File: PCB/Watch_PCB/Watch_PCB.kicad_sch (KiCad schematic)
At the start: 54 parts, among them IC1 PCF2003DUS, IC2 BMM350, IC3 STM32L011E4Y6TR, IC4 TPS22919DCKR, Q11 2N7002KQBZ, Q12 2N7002KQBZ, Q3 2N7002KQBZ, Q4 2N7002KQBZ, Q5 2N7002KQBZ, Q6 2N7002KQBZ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

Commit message: added debounce on switch
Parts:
- added C12: 220n, Capacitor_SMD:C_0201_0603Metric, symbol Device:C
- added R18: 47k, Resistor_SMD:R_0201_0603Metric, symbol Device:R
- R17: value 10k -> 1k
- renumbered CLPT to CLPT1, CSPT to CSPT1
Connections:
- net GND: now also C12.1
- net GPIO_EXTI9: now also R18.2; no longer R17.2, SW5.3 (K), SW5.4 (A)
- new net: C12.2, R17.2, R18.1, SW5.3 (K), SW5.4 (A)
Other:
- moved on the sheet: R17, SW5

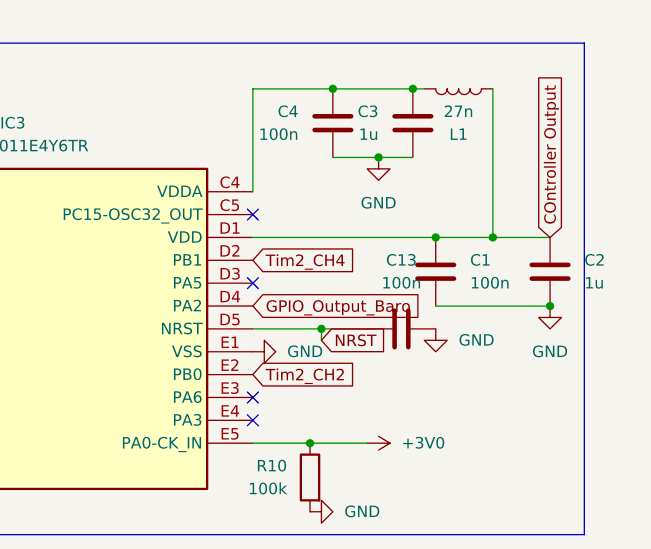
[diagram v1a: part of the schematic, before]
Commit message: pcb outline
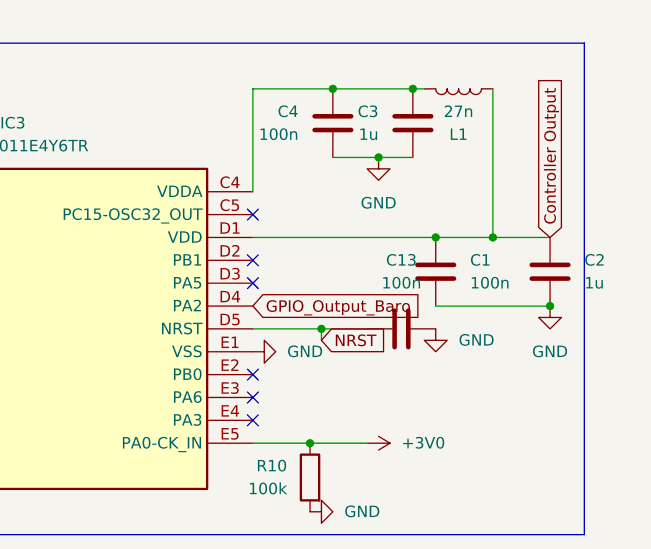
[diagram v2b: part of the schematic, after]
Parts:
- IC4: footprint SOT65P210X110-6N -> SamacSys_Parts:SOT65P210X110-6N
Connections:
- net COntroller Output is gone; now on net Controller Output: C1.2, C2.2, IC3.D1 (VDD), L1.1
- net Tim2_CH2: no longer names the net of IC3.E2 (PB0)
- net Tim2_CH4: no longer names the net of IC3.D2 (PB1)
- no-connect marks 10 -> 12
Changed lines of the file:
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@@
+	)
+	(no_connect
+		(at 241.3 39.37)
 	)
 	(no_connect
@@
 	)
 	(no_connect
+		(at 241.3 52.07)
+	)
+	(no_connect
 		(at 121.92 182.88)
 	)
@@
 		)
 	)
+	(global_label "Controller Output"
+		(shape input)
+		(at 274.32 36.83 90)
+		(fields_autoplaced yes)
+		(effects
+			(font
+				(size 1.27 1.27)
+			)
+			(justify left)
+		)
+		(property "Intersheetrefs" "${INTERSHEET_REFS}"
+			(at 274.32 17.2142 90)
+			(effects
+				(font
+					(size 1.27 1.27)
+				)
+				(justify left)
+				(hide yes)
+			)
+		)
+	)
 	(global_label "SYS_SWCLK"
 		(shape input)
@@
 		)
 	)
-	(global_label "COntroller Output"
-		(shape input)
-		(at 274.32 36.83 90)
+	(global_label "BaroVCC"
+		(shape input)
+		(at 240.03 77.47 0)
 		(fields_autoplaced yes)
 		(effects
@@
 		)
 		(property "Intersheetrefs" "${INTERSHEET_REFS}"
-			(at 274.32 17.0327 90)
+			(at 250.998 77.47 0)
 			(effects
 				(font
@@
 		)
 	)
-	(global_label "BaroVCC"
-		(shape input)
-		(at 240.03 77.47 0)
+	(global_label "OSCIN"
+		(shape input)
+		(at 121.92 187.96 180)
+		(fields_autoplaced yes)
+		(effects
+			(font
+				(size 1.27 1.27)
+			)
+			(justify right)
+		)
+		(property "Intersheetrefs" "${INTERSHEET_REFS}"
+			(at 113.1895 187.96 0)
+			(effects
+				(font
+					(size 1.27 1.27)
+				)
+				(justify right)
+				(hide yes)
+			)
+		)
+	)
+	(global_label "GPIO_EXTI1"
+		(shape input)
+		(at 237.49 137.16 0)
 		(fields_autoplaced yes)
 		(effects
@@
 		)
 		(property "Intersheetrefs" "${INTERSHEET_REFS}"
-			(at 250.998 77.47 0)
+			(at 251.0585 137.16 0)
 			(effects
 				(font
@@
 		)
 	)
+	(global_label "GPIO_EXTI9"
+		(shape input)
+		(at 187.96 41.91 180)
+		(fields_autoplaced yes)
+		(effects
+			(font
+				(size 1.27 1.27)
+			)
+			(justify right)
+		)
+		(property "Intersheetrefs" "${INTERSHEET_REFS}"
+			(at 174.3915 41.91 0)
+			(effects
+				(font
+					(size 1.27 1.27)
+				)
+				(justify right)
+				(hide yes)
+			)
+		)
+	)
+	(global_label "SYS_SWCLK"
+		(shape input)
+		(at 187.96 34.29 180)
+		(fields_autoplaced yes)
+		(effects
+			(font
+				(size 1.27 1.27)
+			)
+			(justify right)
+		)
+		(property "Intersheetrefs" "${INTERSHEET_REFS}"
+			(at 174.2706 34.29 0)
+			(effects
+				(font
+					(size 1.27 1.27)
+				)
+				(justify right)
+				(hide yes)
+			)
+		)
+	)
+	(global_label "GPIO_EXTI9"
+		(shape input)
+		(at 204.47 138.43 0)
+		(fields_autoplaced yes)
+		(effects
+			(font
+				(size 1.27 1.27)
+			)
+			(justify left)
+		)
+		(property "Intersheetrefs" "${INTERSHEET_REFS}"
+			(at 218.0385 138.43 0)
+			(effects
+				(font
+					(size 1.27 1.27)
+				)
+				(justify left)
+				(hide yes)
+			)
+		)
+	)
+	(global_label "Controller Output"
+		(shape input)
+		(at 279.4 130.81 180)
+		(fields_autoplaced yes)
+		(effects
+			(font
+				(size 1.27 1.27)
+			)
+			(justify right)
+		)
+		(property "Intersheetrefs" "${INTERSHEET_REFS}"
+			(at 259.7842 130.81 0)
+			(effects
+				(font
+					(size 1.27 1.27)
+				)
+				(justify right)
+				(hide yes)
+			)
+		)
+	)
+	(global_label "Tim2_CH1"
+		(shape input)
+		(at 158.75 49.53 180)
+		(fields_autoplaced yes)
+		(effects
+			(font
+				(size 1.27 1.27)
+			)
+			(justify right)
+		)
+		(property "Intersheetrefs" "${INTERSHEET_REFS}"
+			(at 146.512 49.53 0)
+			(effects
+				(font
+					(size 1.27 1.27)
+				)
+				(justify right)
+				(hide yes)
+			)
+		)
+	)
 	(global_label "OSCIN"
 		(shape input)
-		(at 121.92 187.96 180)
+		(at 121.92 161.29 180)
 		(fields_autoplaced yes)
 		(effects
@@
 		)
 		(property "Intersheetrefs" "${INTERSHEET_REFS}"
-			(at 113.1895 187.96 0)
+			(at 113.1895 161.29 0)
 			(effects
 				(font
@@
 		)
 	)
-	(global_label "GPIO_EXTI1"
-		(shape input)
-		(at 237.49 137.16 0)
+	(global_label "SYS_SWDIO"
+		(shape input)
+		(at 152.4 21.59 180)
+		(fields_autoplaced yes)
+		(effects
+			(font
+				(size 1.27 1.27)
+			)
+			(justify right)
+		)
+		(property "Intersheetrefs" "${INTERSHEET_REFS}"
+			(at 139.0734 21.59 0)
+			(effects
+				(font
+					(size 1.27 1.27)
+				)
+				(justify right)
+				(hide yes)
+			)
+		)
+	)
+	(global_label "GPIO_Output_Comp"
+		(shape input)
+		(at 135.89 93.98 0)
 		(fields_autoplaced yes)
 		(effects
@@
 		)
 		(property "Intersheetrefs" "${INTERSHEET_REFS}"
-			(at 251.0585 137.16 0)
-			(effects
-				(font
-					(size 1.27 1.27)
-				)
-				(justify left)
-				(hide yes)
-			)
-		)
-	)
-	(global_label "GPIO_EXTI9"
-		(shape input)
-		(at 187.96 41.91 180)
-		(fields_autoplaced yes)
-		(effects
-			(font
-				(size 1.27 1.27)
-			)
-			(justify right)
-		)
-		(property "Intersheetrefs" "${INTERSHEET_REFS}"
-			(at 174.3915 41.91 0)
-			(effects
-				(font
-					(size 1.27 1.27)
-				)
-				(justify right)
-				(hide yes)
-			)
-		)
-	)
-	(global_label "SYS_SWCLK"
-		(shape input)
-		(at 187.96 34.29 180)
-		(fields_autoplaced yes)
-		(effects
-			(font
-				(size 1.27 1.27)
-			)
-			(justify right)
-		)
-		(property "Intersheetrefs" "${INTERSHEET_REFS}"
-			(at 174.2706 34.29 0)
-			(effects
-				(font
-					(size 1.27 1.27)
-				)
-				(justify right)
-				(hide yes)
-			)
-		)
-	)
-	(global_label "GPIO_EXTI9"
-		(shape input)
-		(at 204.47 138.43 0)
-		(fields_autoplaced yes)
-		(effects
-			(font
-				(size 1.27 1.27)
-			)
-			(justify left)
-		)
-		(property "Intersheetrefs" "${INTERSHEET_REFS}"
-			(at 218.0385 138.43 0)
-			(effects
-				(font
-					(size 1.27 1.27)
-				)
-				(justify left)
-				(hide yes)
-			)
-		)
-	)
-	(global_label "Controller Output"
-		(shape input)
-		(at 279.4 130.81 180)
-		(fields_autoplaced yes)
-		(effects
-			(font
-				(size 1.27 1.27)
-			)
-			(justify right)
-		)
-		(property "Intersheetrefs" "${INTERSHEET_REFS}"
-			(at 259.7842 130.81 0)
-			(effects
-				(font
-					(size 1.27 1.27)
-				)
-				(justify right)
-				(hide yes)
-			)
-		)
-	)
-	(global_label "Tim2_CH1"
-		(shape input)
-		(at 158.75 49.53 180)
-		(fields_autoplaced yes)
-		(effects
-			(font
-				(size 1.27 1.27)
-			)
-			(justify right)
-		)
-		(property "Intersheetrefs" "${INTERSHEET_REFS}"
-			(at 146.512 49.53 0)
-			(effects
-				(font
-					(size 1.27 1.27)
-				)
-				(justify right)
-				(hide yes)
-			)
-		)
-	)
-	(global_label "OSCIN"
-		(shape input)
-		(at 121.92 161.29 180)
-		(fields_autoplaced yes)
-		(effects
-			(font
-				(size 1.27 1.27)
-			)
-			(justify right)
-		)
-		(property "Intersheetrefs" "${INTERSHEET_REFS}"
-			(at 113.1895 161.29 0)
-			(effects
-				(font
-					(size 1.27 1.27)
-				)
-				(justify right)
-				(hide yes)
-			)
-		)
-	)
-	(global_label "SYS_SWDIO"
-		(shape input)
-		(at 152.4 21.59 180)
-		(fields_autoplaced yes)
-		(effects
-			(font
-				(size 1.27 1.27)
-			)
-			(justify right)
-		)
-		(property "Intersheetrefs" "${INTERSHEET_REFS}"
-			(at 139.0734 21.59 0)
-			(effects
-				(font
-					(size 1.27 1.27)
-				)
-				(justify right)
-				(hide yes)
-			)
-		)
-	)
-	(global_label "Tim2_CH2"
-		(shape input)
-		(at 241.3 52.07 0)
-		(fields_autoplaced yes)
-		(effects
-			(font
-				(size 1.27 1.27)
-			)
-			(justify left)
-		)
-		(property "Intersheetrefs" "${INTERSHEET_REFS}"
-			(at 253.538 52.07 0)
-			(effects
-				(font
-					(size 1.27 1.27)
-				)
-				(justify left)
-				(hide yes)
-			)
-		)
-	)
-	(global_label "GPIO_Output_Comp"
-		(shape input)
-		(at 135.89 93.98 0)
-		(fields_autoplaced yes)
-		(effects
-			(font
-				(size 1.27 1.27)
-			)
-			(justify left)
-		)
-		(property "Intersheetrefs" "${INTERSHEET_REFS}"
 			(at 156.7759 93.98 0)
-			(effects
-				(font
-					(size 1.27 1.27)
-				)
-				(justify left)
-				(hide yes)
-			)
-		)
-	)
-	(global_label "Tim2_CH4"
-		(shape input)
-		(at 241.3 39.37 0)
-		(fields_autoplaced yes)
-		(effects
-			(font
-				(size 1.27 1.27)
-			)
-			(justify left)
-		)
-		(property "Intersheetrefs" "${INTERSHEET_REFS}"
-			(at 253.538 39.37 0)
 			(effects
 				(font
@@
 			)
 		)
-		(property "Footprint" "SOT65P210X110-6N"
+		(property "Footprint" "SamacSys_Parts:SOT65P210X110-6N"
 			(at 267.97 237.16 0)
 			(effects

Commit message: pcb layout
pcb layout
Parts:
- removed IC4: TPS22919DCKR, SamacSys_Parts:SOT65P210X110-6N, symbol SamacSys_Parts:TPS22919DCKR
- removed Q11, Q12: 2N7002KQBZ, SamacSys_Parts:2N7002KQBZ, symbol SamacSys_Parts:2N7002KQBZ
- removed R6, R7: 2k, Resistor_SMD:R_0201_0603Metric, symbol Device:R
- added IC4: TPS22991BRAAR, SamacSys_Parts:TPS22991BRAAR, symbol SamacSys_Parts:TPS22991BRAAR
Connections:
- net BaroVCC is gone; now on net Controller Output: C5.1, C9.1, IC2.B3 (VDDIO), IC2.C1 (VDD), R4.1, R5.1
- net CompVCC is gone; now on net Controller Output: C11.2, U1.10 (VDD)
- net +3V0: now also SW5.3 (K), SW5.4 (A), IC4.1 (VIN); no longer SW5.1, SW5.2
- net Controller Output: now also IC4.3 (VOUT)
- net GND: now also IC4.4 (GND)
- net at TPS3424-1.6 (RESET/~RESET~): now also IC4.2 (ON)
- net at C12.2, R17.2, R18.1: now also SW5.1, SW5.2; no longer SW5.3 (K), SW5.4 (A)
- net GPIO_Output_Baro: no longer names the net of IC3.D4 (PA2)
- net GPIO_Output_Comp: no longer names the net of IC3.B2 (PB3)
- no-connect marks 12 -> 14
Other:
- moved on the sheet: SW5

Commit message: PCB V1
PCB V1 complete
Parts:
- removed TP3, TP4: MOT, TestPoint:TestPoint_Pad_D1.0mm, symbol Connector:TestPoint
- removed TP8: SD1+, TestPoint:TestPoint_Pad_D1.0mm, symbol Connector:TestPoint
- removed TP9: SD1-, TestPoint:TestPoint_Pad_D1.0mm, symbol Connector:TestPoint
- added L2, L3: L, SamacSys_Parts:Miyota 2035, symbol Device:L
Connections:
- net GND: now also Y1.4 (NC)
- net at Q4.3 (D_1), Q4.4 (D_2), Q6.2 (S)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: now also L2.2
- net at IC1.B4 (MOT2): now also L3.1
- net at Q3.3 (D_1), Q3.4 (D_2), Q5.2 (S)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: now also L2.1
- net at IC1.C3 (MOT1): now also L3.2
